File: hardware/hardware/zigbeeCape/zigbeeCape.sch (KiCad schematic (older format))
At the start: 46 parts, among them J1 Conn_ARM_JTAG_SWD_10, SW1 SW_MEC_5E, SW2 SW_MEC_5E, SW3 SW_MEC_5E, SW4 SW_MEC_5E, SW5 SW_MEC_5E, U1 CC1352R, Y1 32.768kHz, Y2 48MHz

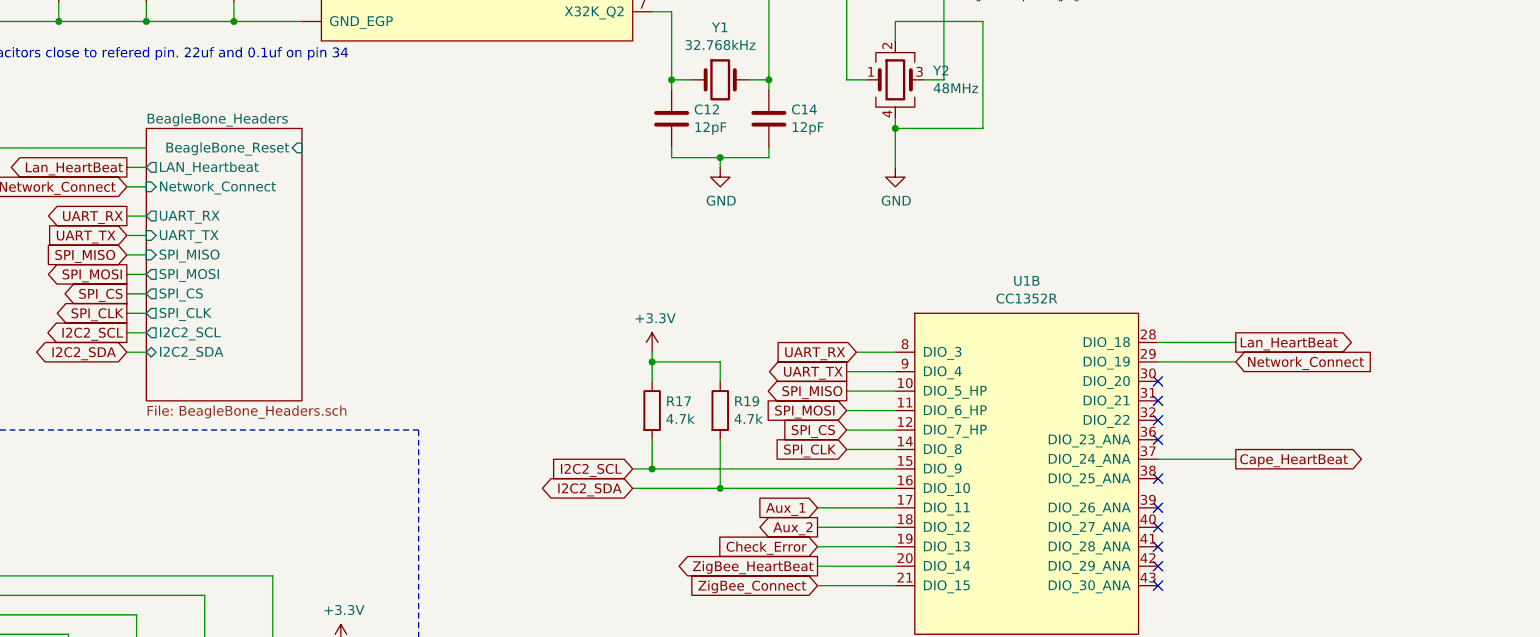
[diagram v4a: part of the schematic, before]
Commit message: Setup DRC, completed coms lines
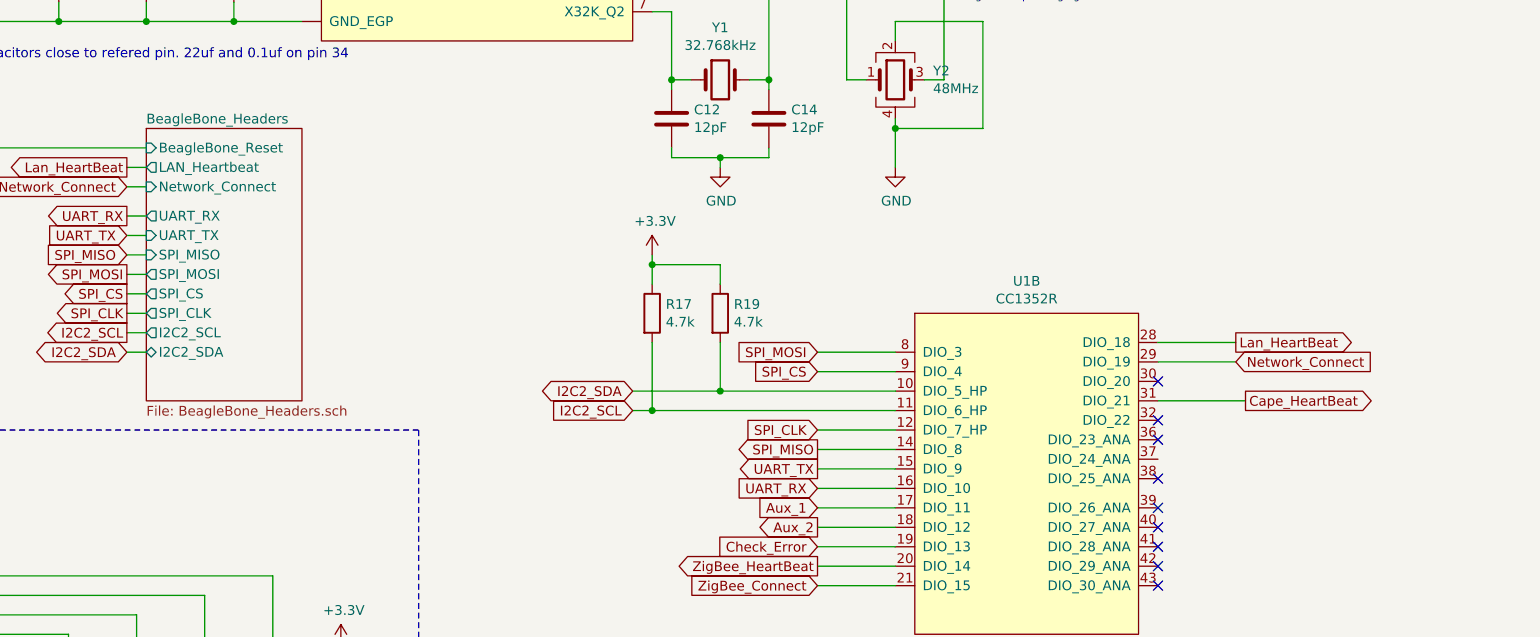
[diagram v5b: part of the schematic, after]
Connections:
- net BeagleBone_Headers/BeagleBone_Reset: now also C4.1, R1.2, SW4.3 (K), SW4.4 (A)
- net Cape_HeartBeat: now also U1.31 (DIO_21); no longer U1.37 (DIO_24_ANA)
- net I2C2_SCL: now also U1.11 (DIO_6_HP); no longer U1.15 (DIO_9)
- net I2C2_SDA: now also U1.10 (DIO_5_HP); no longer U1.16 (DIO_10)
- net SPI_CLK: now also U1.12 (DIO_7_HP); no longer U1.14 (DIO_8)
- net SPI_CS: now also U1.9 (DIO_4); no longer U1.12 (DIO_7_HP)
- net SPI_MISO: now also U1.14 (DIO_8); no longer U1.10 (DIO_5_HP)
- net SPI_MOSI: now also U1.8 (DIO_3); no longer U1.11 (DIO_6_HP)
- net UART_RX: now also U1.16 (DIO_10); no longer U1.8 (DIO_3)
- net UART_TX: now also U1.15 (DIO_9); no longer U1.9 (DIO_4)
- no-connect marks 10 -> 9
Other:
- moved on the sheet: R17, R19
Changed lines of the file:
@@
 F6 "2_4_GHZ_RF_P" I L 8000 1750 50
-$EndSheet
-$Sheet
-S 4000 3750 800  1400
-U 6087B849
-F0 "BeagleBone_Headers" 50
-F1 "BeagleBone_Headers.sch" 50
-F2 "BeagleBone_Reset" I R 4800 3850 50
-F3 "LAN_Heartbeat" O L 4000 3950 50
-F4 "SPI_MISO" I L 4000 4400 50
-F5 "SPI_MOSI" O L 4000 4500 50
-F6 "SPI_CS" O L 4000 4600 50
-F7 "Network_Connect" I L 4000 4050 50
-F8 "UART_RX" O L 4000 4200 50
-F9 "UART_TX" I L 4000 4300 50
-F10 "SPI_CLK" O L 4000 4700 50
-F11 "I2C2_SCL" O L 4000 4800 50
-F12 "I2C2_SDA" B L 4000 4900 50
 $EndSheet
 Wire Wire Line
@@
 Wire Wire Line
 	3900 4200 4000 4200
-Text GLabel 7650 4900 0    50   Input ~ 0
+Text GLabel 7450 5600 0    50   Input ~ 0
 UART_RX
-Text GLabel 7600 5000 0    50   Output ~ 0
+Text GLabel 7450 5500 0    50   Output ~ 0
 UART_TX
-Text GLabel 7600 5100 0    50   Output ~ 0
+Text GLabel 7450 5400 0    50   Output ~ 0
 SPI_MISO
-Text GLabel 7600 5200 0    50   Input ~ 0
+Text GLabel 7450 4900 0    50   Input ~ 0
 SPI_MOSI
-Text GLabel 7600 5300 0    50   Input ~ 0
+Text GLabel 7450 5000 0    50   Input ~ 0
 SPI_CS
-Text GLabel 7600 5400 0    50   Input ~ 0
+Text GLabel 7450 5300 0    50   Input ~ 0
 SPI_CLK
 Text Notes 2900 3400 0    50   ~ 0
@@
 L Device:R R19
 U 1 1 608B8299
-P 6950 5200
-F 0 "R19" H 7020 5246 50  0000 L CNN
-F 1 "4.7k" H 7020 5155 50  0000 L CNN
-F 2 "Resistor_SMD:R_0603_1608Metric_Pad0.98x0.95mm_HandSolder" V 6880 5200 50  0001 C CNN
-F 3 "~" H 6950 5200 50  0001 C CNN
-	1    6950 5200
+P 6950 4700
+F 0 "R19" H 7020 4746 50  0000 L CNN
+F 1 "4.7k" H 7020 4655 50  0000 L CNN
+F 2 "Resistor_SMD:R_0603_1608Metric_Pad0.98x0.95mm_HandSolder" V 6880 4700 50  0001 C CNN
+F 3 "~" H 6950 4700 50  0001 C CNN
+	1    6950 4700
 	1    0    0    -1
 $EndComp
@@
 L Device:R R17
 U 1 1 608B8AB3
-P 6600 5200
-F 0 "R17" H 6670 5246 50  0000 L CNN
-F 1 "4.7k" H 6670 5155 50  0000 L CNN
-F 2 "Resistor_SMD:R_0603_1608Metric_Pad0.98x0.95mm_HandSolder" V 6530 5200 50  0001 C CNN
-F 3 "~" H 6600 5200 50  0001 C CNN
-	1    6600 5200
+P 6600 4700
+F 0 "R17" H 6670 4746 50  0000 L CNN
+F 1 "4.7k" H 6670 4655 50  0000 L CNN
+F 2 "Resistor_SMD:R_0603_1608Metric_Pad0.98x0.95mm_HandSolder" V 6530 4700 50  0001 C CNN
+F 3 "~" H 6600 4700 50  0001 C CNN
+	1    6600 4700
 	1    0    0    -1
 $EndComp
@@
 L power:+3.3V #PWR028
 U 1 1 608BA24C
-P 6600 4900
-F 0 "#PWR028" H 6600 4750 50  0001 C CNN
-F 1 "+3.3V" H 6615 5073 50  0000 C CNN
-F 2 "" H 6600 4900 50  0001 C CNN
-F 3 "" H 6600 4900 50  0001 C CNN
-	1    6600 4900
-	1    0    0    -1
-$EndComp
-Text GLabel 6500 5500 0    50   Input ~ 0
+P 6600 4400
+F 0 "#PWR028" H 6600 4250 50  0001 C CNN
+F 1 "+3.3V" H 6615 4573 50  0000 C CNN
+F 2 "" H 6600 4400 50  0001 C CNN
+F 3 "" H 6600 4400 50  0001 C CNN
+	1    6600 4400
+	1    0    0    -1
+$EndComp
+Text GLabel 6500 5200 0    50   Input ~ 0
 I2C2_SCL
-Text GLabel 6500 5600 0    50   BiDi ~ 0
+Text GLabel 6500 5100 0    50   BiDi ~ 0
 I2C2_SDA
 $Comp
@@
 	4900 900  4900 1000
 Connection ~ 4900 900
-Text GLabel 9600 5450 2    50   Output ~ 0
+Text GLabel 9650 5150 2    50   Output ~ 0
 Cape_HeartBeat
 $Comp
@@
 	7850 3750 7850 3700
 Connection ~ 7850 3750
-Wire Wire Line
-	7650 4900 7850 4900
-Wire Wire Line
-	7850 5000 7600 5000
-Wire Wire Line
-	7600 5100 7850 5100
-Wire Wire Line
-	7850 5200 7600 5200
-Wire Wire Line
-	7600 5300 7850 5300
-Wire Wire Line
-	7850 5400 7600 5400
 Text Notes 8200 3100 0    39   ~ 0
 This symbol looks gross.\nMight endup changing it.
@@
 	7850 5700 7450 5700
 Wire Wire Line
-	7850 5600 6950 5600
-Wire Wire Line
-	6500 5500 6600 5500
-Wire Wire Line
-	6950 5350 6950 5600
-Connection ~ 6950 5600
-Wire Wire Line
-	6950 5600 6500 5600
-Wire Wire Line
-	6600 5500 6600 5350
-Connection ~ 6600 5500
-Wire Wire Line
-	6600 5500 7850 5500
-Wire Wire Line
-	6950 5050 6950 4950
-Wire Wire Line
-	6950 4950 6600 4950
-Wire Wire Line
-	6600 4950 6600 4900
-Wire Wire Line
-	6600 5050 6600 4950
-Connection ~ 6600 4950
+	6950 4550 6950 4450
+Wire Wire Line
+	6950 4450 6600 4450
+Wire Wire Line
+	6600 4450 6600 4400
+Wire Wire Line
+	6600 4550 6600 4450
+Connection ~ 6600 4450
 Wire Wire Line
 	9200 4850 9600 4850
 Wire Wire Line
 	9600 4950 9200 4950
-Wire Wire Line
-	9200 5450 9600 5450
 NoConn ~ 9200 5050
-NoConn ~ 9200 5150
 NoConn ~ 9200 5250
 NoConn ~ 9200 5350
@@
 Wire Wire Line
 	7850 6100 7450 6100
+Wire Wire Line
+	9200 5150 9650 5150
+Wire Wire Line
+	7450 5600 7850 5600
+Wire Wire Line
+	7450 5500 7850 5500
+Wire Wire Line
+	7450 5400 7850 5400
+Wire Wire Line
+	7450 5300 7850 5300
+Wire Wire Line
+	7450 5000 7850 5000
+Wire Wire Line
+	7450 4900 7850 4900
+Wire Wire Line
+	6500 5200 6600 5200
+Wire Wire Line
+	6500 5100 6950 5100
+Wire Wire Line
+	6950 4850 6950 5100
+Connection ~ 6950 5100
+Wire Wire Line
+	6950 5100 7850 5100
+Wire Wire Line
+	6600 4850 6600 5200
+Connection ~ 6600 5200
+Wire Wire Line
+	6600 5200 7850 5200
+$Sheet
+S 4000 3750 800  1400
+U 6087B849
+F0 "BeagleBone_Headers" 50
+F1 "BeagleBone_Headers.sch" 50
+F2 "BeagleBone_Reset" I L 4000 3850 50
+F3 "LAN_Heartbeat" O L 4000 3950 50
+F4 "SPI_MISO" I L 4000 4400 50
+F5 "SPI_MOSI" O L 4000 4500 50
+F6 "SPI_CS" O L 4000 4600 50
+F7 "Network_Connect" I L 4000 4050 50
+F8 "UART_RX" O L 4000 4200 50
+F9 "UART_TX" I L 4000 4300 50
+F10 "SPI_CLK" O L 4000 4700 50
+F11 "I2C2_SCL" O L 4000 4800 50
+F12 "I2C2_SDA" B L 4000 4900 50
+$EndSheet
 $EndSCHEMATC

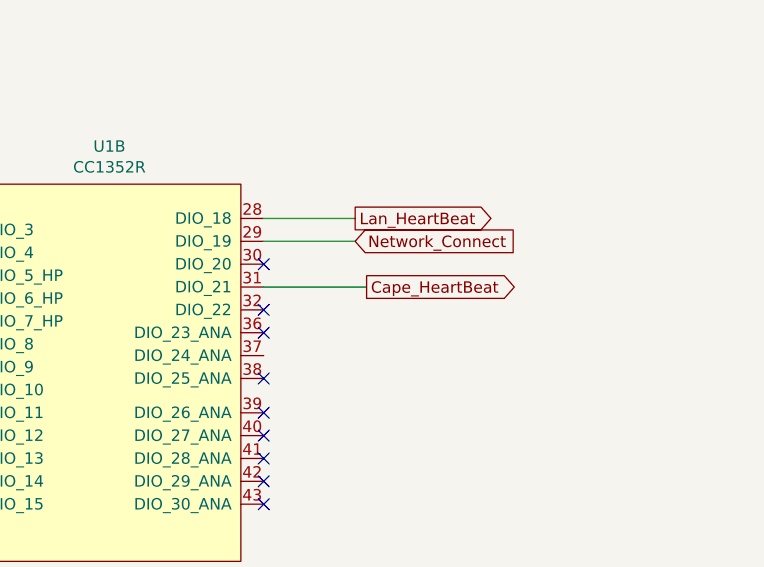
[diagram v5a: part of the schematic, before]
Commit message: Fixed a couple schematic symbols
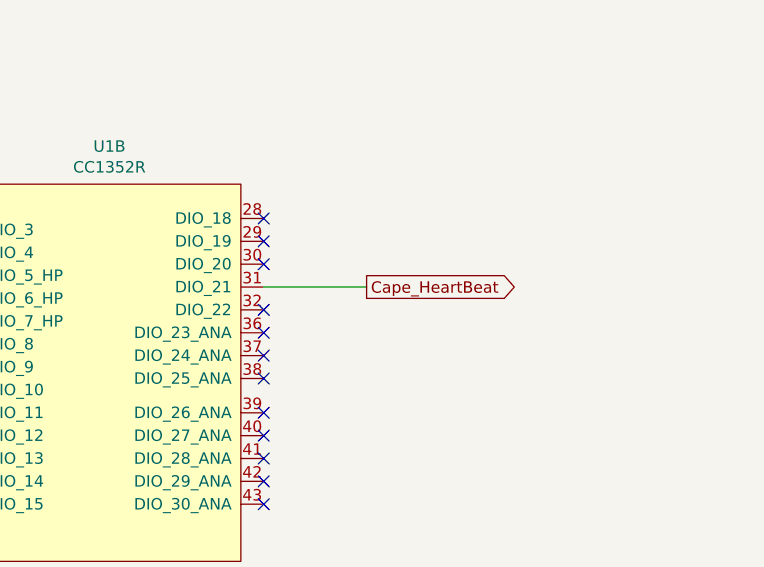
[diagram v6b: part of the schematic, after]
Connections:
- net Lan_HeartBeat: no longer U1.28 (DIO_18)
- net Network_Connect: no longer U1.29 (DIO_19)
- no-connect marks 9 -> 12
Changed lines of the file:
@@
 Text GLabel 3900 4400 0    50   Input ~ 0
 SPI_MISO
-Text GLabel 9600 4950 2    50   Input ~ 0
-Network_Connect
-Text GLabel 9600 4850 2    50   Output ~ 0
-Lan_HeartBeat
 Text GLabel 7450 6100 0    50   Input ~ 0
 ZigBee_Connect
@@
 	6600 4550 6600 4450
 Connection ~ 6600 4450
-Wire Wire Line
-	9200 4850 9600 4850
-Wire Wire Line
-	9600 4950 9200 4950
 NoConn ~ 9200 5050
 NoConn ~ 9200 5250
@@
 F12 "I2C2_SDA" B L 4000 4900 50
 $EndSheet
+NoConn ~ 9200 4950
+NoConn ~ 9200 4850
+NoConn ~ 9200 5450
 $EndSCHEMATC

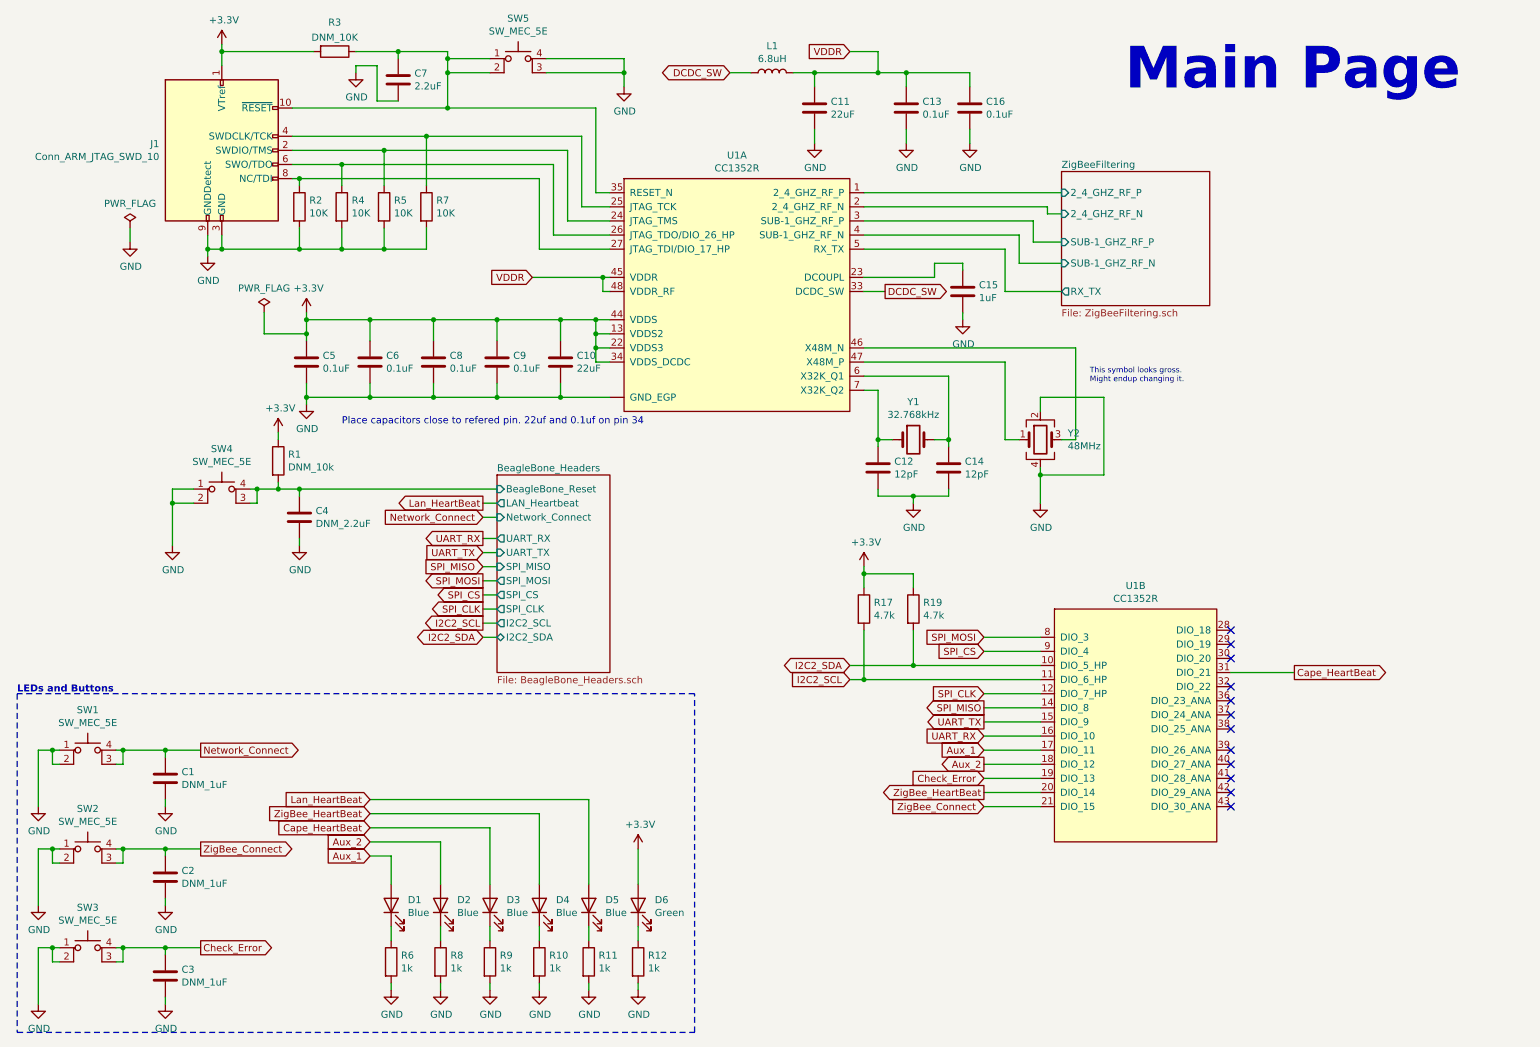
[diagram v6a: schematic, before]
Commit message: Post layout review 1 changes
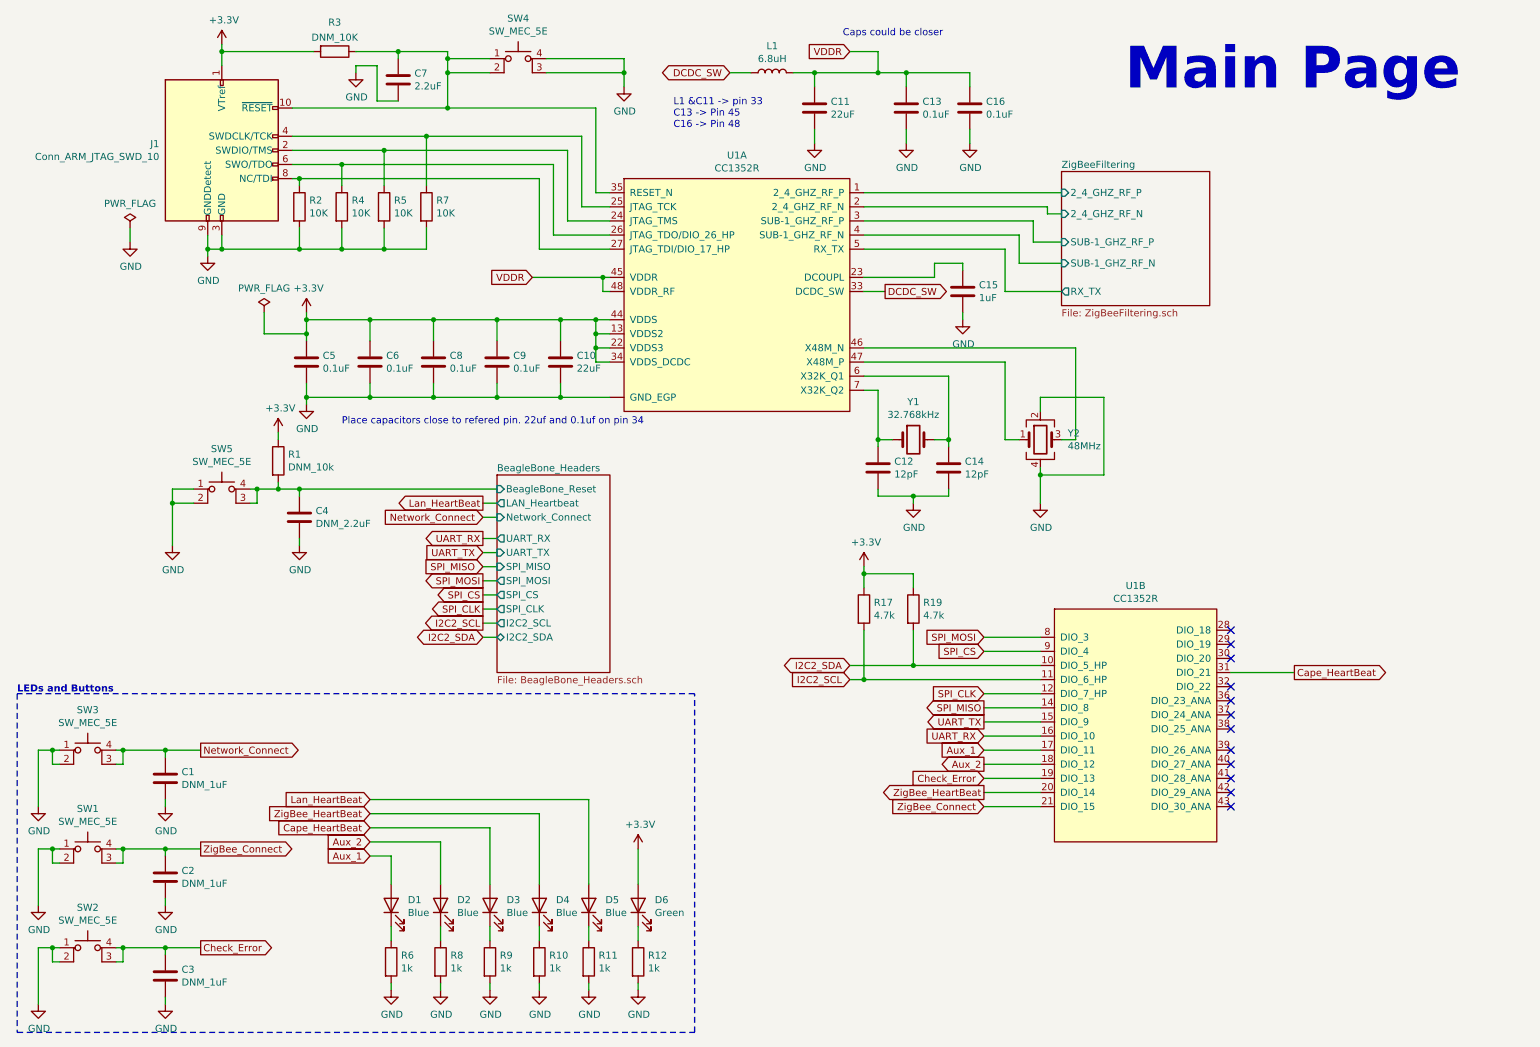
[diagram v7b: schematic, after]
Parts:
- renumbered SW2 to SW1, SW3 to SW2, SW1 to SW3, SW5 to SW4, SW4 to SW5
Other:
- note added: "Caps could be closer"
- note added: "L1 &C11 -> pin 33\nC13 -> Pin 45\nC16 -> Pin 48"
- note removed: "This symbol looks gross.\nMight endup changing it."
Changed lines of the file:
@@
 $EndComp
 $Comp
-L Switch:SW_MEC_5E SW1
+L Switch:SW_MEC_5E SW3
 U 1 1 606B9FBA
 P 1100 5800
-F 0 "SW1" H 1100 6185 50  0000 C CNN
+F 0 "SW3" H 1100 6185 50  0000 C CNN
 F 1 "SW_MEC_5E" H 1100 6094 50  0000 C CNN
 F 2 "zigbeeCape:SMD_PUSH_BUTTON" H 1100 6100 50  0001 C CNN
@@
 Connection ~ 850  5700
 $Comp
-L Switch:SW_MEC_5E SW2
+L Switch:SW_MEC_5E SW1
 U 1 1 606D1A3D
 P 1100 6500
-F 0 "SW2" H 1100 6885 50  0000 C CNN
+F 0 "SW1" H 1100 6885 50  0000 C CNN
 F 1 "SW_MEC_5E" H 1100 6794 50  0000 C CNN
 F 2 "zigbeeCape:SMD_PUSH_BUTTON" H 1100 6800 50  0001 C CNN
@@
 Connection ~ 850  6400
 $Comp
-L Switch:SW_MEC_5E SW3
+L Switch:SW_MEC_5E SW2
 U 1 1 606D3527
 P 1100 7200
-F 0 "SW3" H 1100 7585 50  0000 C CNN
+F 0 "SW2" H 1100 7585 50  0000 C CNN
 F 1 "SW_MEC_5E" H 1100 7494 50  0000 C CNN
 F 2 "zigbeeCape:SMD_PUSH_BUTTON" H 1100 7500 50  0001 C CNN
@@
 	3200 2150 3500 2150
 $Comp
-L Switch:SW_MEC_5E SW5
+L Switch:SW_MEC_5E SW4
 U 1 1 60A32575
 P 4150 900
-F 0 "SW5" H 4150 1285 50  0000 C CNN
+F 0 "SW4" H 4150 1285 50  0000 C CNN
 F 1 "SW_MEC_5E" H 4150 1194 50  0000 C CNN
 F 2 "zigbeeCape:SMD_PUSH_BUTTON" H 4150 1200 50  0001 C CNN
@@
 	4900 800  4900 900
 $Comp
-L Switch:SW_MEC_5E SW4
+L Switch:SW_MEC_5E SW5
 U 1 1 60A76337
 P 2050 3950
-F 0 "SW4" H 2050 4335 50  0000 C CNN
+F 0 "SW5" H 2050 4335 50  0000 C CNN
 F 1 "SW_MEC_5E" H 2050 4244 50  0000 C CNN
 F 2 "zigbeeCape:SMD_PUSH_BUTTON" H 2050 4250 50  0001 C CNN
@@
 	7850 3750 7850 3700
 Connection ~ 7850 3750
-Text Notes 8200 3100 0    39   ~ 0
-This symbol looks gross.\nMight endup changing it.
 Text GLabel 3900 4400 0    50   Input ~ 0
 SPI_MISO
@@
 NoConn ~ 9200 4850
 NoConn ~ 9200 5450
+Text Notes 6450 650  0    50   ~ 0
+Caps could be closer
+Text Notes 5250 1300 0    50   ~ 0
+L1 &C11 -> pin 33\nC13 -> Pin 45\nC16 -> Pin 48
 $EndSCHEMATC
